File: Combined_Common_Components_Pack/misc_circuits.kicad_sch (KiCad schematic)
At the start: 26 parts, among them Q10 2N7002K, Q11 2N7002K, Q9 PMOS, U8 FM8002

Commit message: More circuits
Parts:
- removed PROG2: SW_Push, Button_Switch_SMD:SW_SPST_PTS647_Sx38, symbol Switch:SW_Push
- added Batt3: Conn_01x02_Socket, Connector_Molex:Molex_KK-254_AE-6410-02A_1x02_P2.54mm_Vertical, symbol Connector:Conn_01x02_Socket
- added C47: 1nF, Capacitor_SMD:C_0805_2012Metric, symbol 1_Library_GF:C_THT_RECT
- added C48: 10u, Capacitor_SMD:C_0805_2012Metric, symbol Device:C
- added C49: 47nF, Capacitor_THT:C_Rect_L11.0mm_W4.3mm_P10.00mm_MKT, symbol 1_Library_GF:C_THT_RECT
- added C50: 10nF, Capacitor_THT:C_Rect_L7.0mm_W3.5mm_P5.00mm, symbol 1_Library_GF:C_THT_RECT
- added C51: 100n, Capacitor_SMD:C_0603_1608Metric, symbol Device:C
- added D28, D30, D31, D32, D33: SM4007, Diode_SMD:D_MELF, symbol Diode:SM4007
- added D29: LED, LED_SMD:LED_0805_2012Metric_Pad1.15x1.40mm_HandSolder, symbol Device:LED
- added D36, D37: LED, LED_SMD:LED_0805_2012Metric, symbol Device:LED
- added D38, D39: PTVS5V0Z1USK, Diode_SMD:Nexperia_DSN1608-2_1.6x0.8mm, symbol Diode:PTVS5V0Z1USK
- added LOAD1: Conn_01x02_Pin, Connector_Phoenix_GMSTB:PhoenixContact_GMSTBA_2,5_2-G-7,62_1x02_P7.62mm_Horizontal, symbol Connector:Conn_01x02_Pin
- added P1: USB_C_Plug_USB2.0, Connector_USB:USB_C_Receptacle_HRO_TYPE-C-31-M-12, symbol Connector:USB_C_Plug_USB2.0
- added Q13: BTA16-600B, Package_TO_SOT_THT:TO-220-3_Vertical, symbol Triac_Thyristor:BTA16-600B
- added Q14: BC817, Package_TO_SOT_SMD:SOT-23, symbol Transistor_BJT:BC817
- added Q15: 2N7002K, Package_TO_SOT_SMD:SOT-23, symbol Transistor_FET:2N7002K
- added Q16: FDS9926A, Package_SO:SOIC-8_3.9x4.9mm_P1.27mm, symbol Transistor_FET:FDS9926A
- added R100: 22k, Resistor_SMD:R_0805_2012Metric, symbol Device:R
- added R101: 10k, Resistor_SMD:R_0805_2012Metric, symbol Device:R
- added R102, R96: 360, Resistor_THT:R_Axial_DIN0411_L9.9mm_D3.6mm_P15.24mm_Horizontal, symbol Device:R
- added R103: 0R22, Resistor_SMD:R_2010_5025Metric, symbol Device:R
- added R104: 100, Resistor_SMD:R_0603_1608Metric, symbol Device:R
- added R105, R106, R109: 1k, Resistor_SMD:R_0603_1608Metric, symbol Device:R
- added R107, R108: 5k6, Resistor_SMD:R_0603_1608Metric, symbol Device:R
- added R110: 2k2, Resistor_SMD:R_0603_1608Metric, symbol Device:R
- added R90, R98: 220k, Resistor_SMD:R_0805_2012Metric, symbol Device:R
- added R91, R97: 1k, Resistor_SMD:R_0805_2012Metric, symbol Device:R
- added R92, R93, R94: 330, Resistor_SMD:R_0805_2012Metric, symbol Device:R
- added R95: 470, Resistor_THT:R_Axial_DIN0411_L9.9mm_D3.6mm_P15.24mm_Horizontal, symbol Device:R
- added R99: 39, Resistor_THT:R_Axial_DIN0411_L9.9mm_D3.6mm_P15.24mm_Horizontal, symbol Device:R
- added U13: PC817, Package_DIP:SMDIP-4_W7.62mm, symbol Isolator:PC817
- added U18: ~, Library:HEATSINK-TH_L34.0-W12.0, symbol New_Library:Heat Sink 34X12-25
- added U2: MOC3021M, Package_DIP:SMDIP-6_W9.53mm, symbol Relay_SolidState:MOC3021M
- added U20: TP4057, Package_TO_SOT_SMD:TSOT-23-5, symbol Battery_Management:TP4057
- added U21: DW01A, Package_TO_SOT_SMD:SOT-23-6, symbol Battery_Management:DW01A
- U8: Manufacturer FM(富满) -> (none); Supplier LCSC -> (none); Supplier Part C94625 -> (none)
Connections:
- net +3.3V: now also D29.2 (A), R92.1, R93.1
- net +BATT: now also Batt3.1 (Pin_1), R104.2, U20.3 (BAT)
- net GND: now also D38.2 (A), D39.2 (A), P1.A1 (GND), P1.A12 (GND), P1.B1 (GND), P1.B12 (GND), P1.S1 (SHIELD), Q15.2 (S), Q16.1 (S1), R101.2, R107.1, R108.1, R109.1, R110.1, U13.3, U20.2 (GND)
- new net: C47.1, D30.2 (A), D31.1 (K), R98.1
- new net: D31.2 (A), D32.1 (K), D33.2 (A), Q14.1 (B), R100.2
- new net: R105.1, U20.5 (STDBY)
- new net: D36.1 (K), R105.2
- new net: LOAD1.2 (Pin_2), Q13.2 (A2), R96.2, R99.2
- new net: Q13.3 (G), R102.2, U2.4
- new net: Q15.1 (G), R101.1, R94.2
- new net: Q16.4 (G2), U21.1 (OD)
- new net: R109.2, U21.2 (CS)
- new net: Q16.2 (G1), U21.3 (OC)
- new net: C51.1, R104.1, U21.5 (VCC)
- new net: Batt3.2 (Pin_2), C51.2, Q16.3 (S2), U21.6 (GND)
- new net: C48.1, D28.1 (K), D30.1 (K), R100.1, R91.1
- new net: C47.2, D28.2 (A), D33.1 (K), R90.1
- new net: R91.2, U13.1
- new net: Q14.3 (C), U13.2
- new net: P1.B5 (VCONN), R107.2
- new net: R106.1, U20.1 (~{CHRG})
- new net: D37.1 (K), R106.2
- new net: Q16.5 (D2), Q16.6 (D2), Q16.7 (D1), Q16.8 (D1)
- new net: C50.2, R99.1
- new net: C48.2, D32.2 (A), Q14.2 (E)
- new net: R92.2, R93.2, U2.1
- new net: Q15.3 (D), U2.2
- new net: R95.2, U2.6
- new net: P1.A5 (CC), R108.2
- new net: C49.1, R95.1, R96.1
- new net: R110.2, U20.6 (PROG)
- new net: R103.2, U20.4 (V_{CC})
- new net: D29.1 (K), R97.2
- new net D+: D38.1 (K), P1.A6 (D+)
- new net D-: D39.1 (K), P1.A7 (D-)
- new net TRIAC: R94.1
- new net VBUS: D36.2 (A), D37.2 (A), P1.A4 (VBUS), P1.A9 (VBUS), P1.B4 (VBUS), P1.B9 (VBUS), R103.1
- new net cold: LOAD1.1 (Pin_1), R98.2
- new net hot: C49.2, C50.1, Q13.1 (A1), R102.1, R90.2
- new net mainDet: R97.1, U13.4
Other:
- note added: "12P USB-C 1S charger + BMS"
- note added: "Auto reset serial programmer"
- note added: "V(AC) Driver"
- note added: "Zero-crossing detector"
- note removed: "Auto reset"
- moved on the sheet: C35, C36, C37, C38, C44, C46, D20, D25, PROG1, Q9, R73, R74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

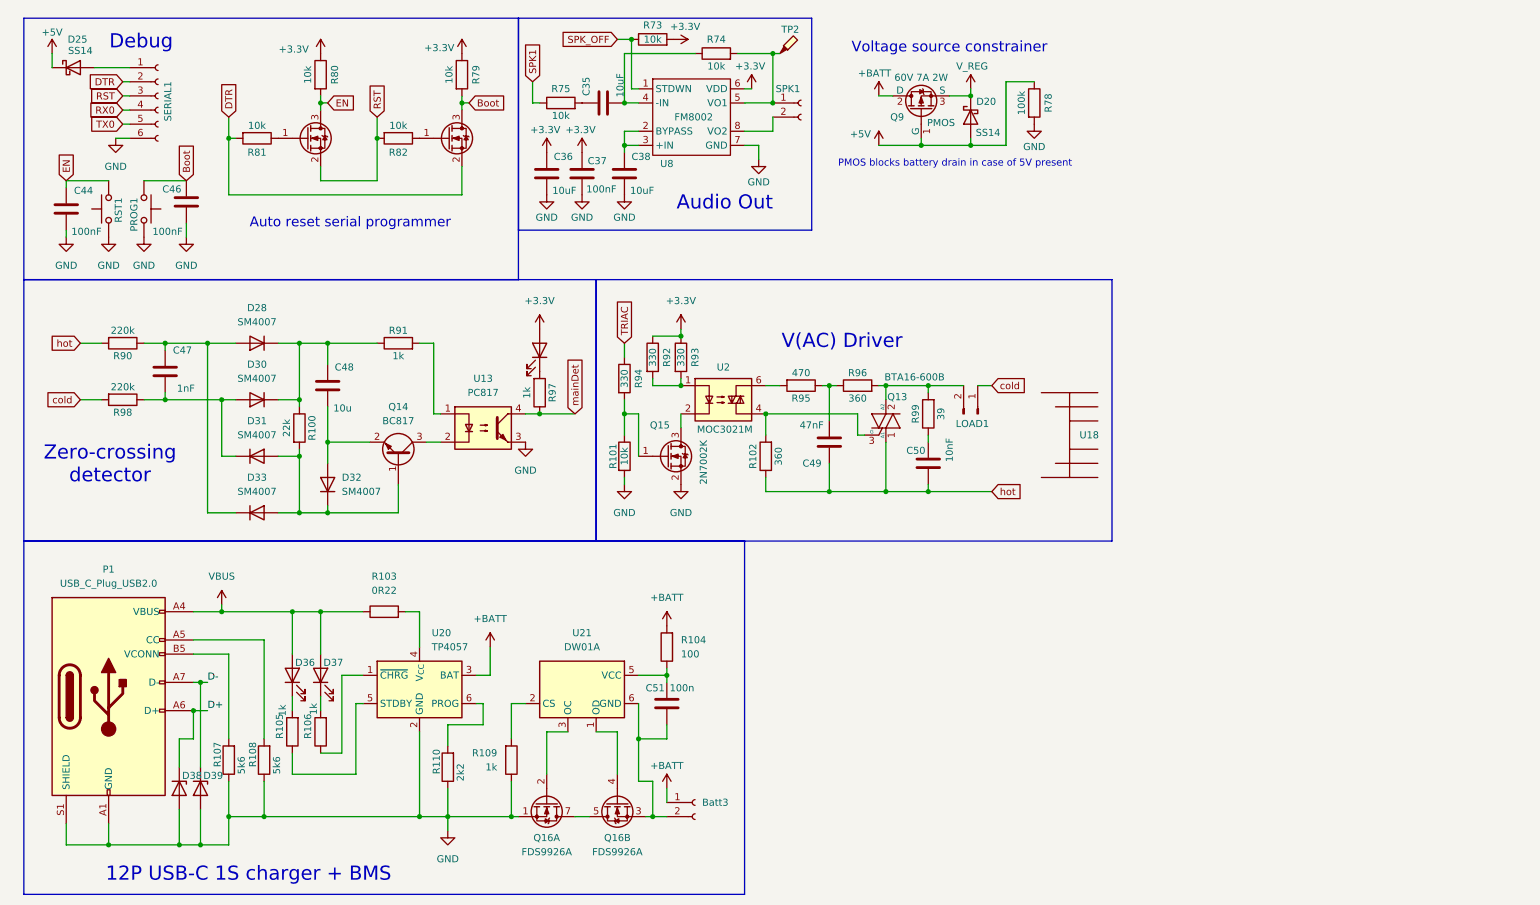
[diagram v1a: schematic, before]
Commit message: Minor updates
Basically components annotation, and more basic parts added
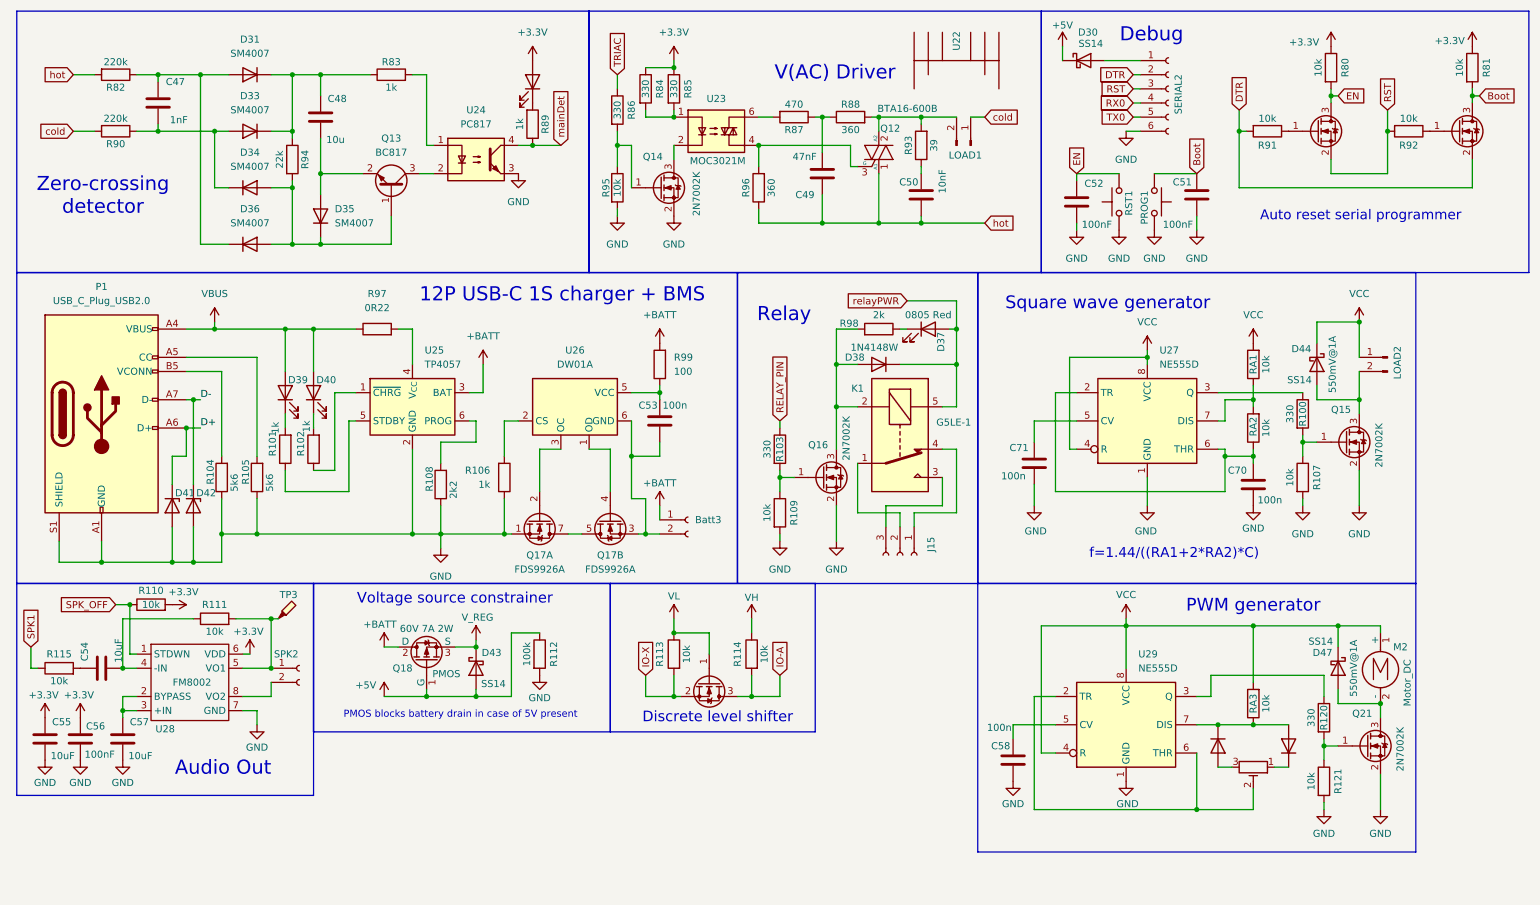
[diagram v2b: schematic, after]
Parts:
- added C58, C70, C71: 100n, Capacitor_SMD:C_0805_2012Metric, symbol Device:C
- added D37: LED_RED, LED_SMD:LED_0805_2012Metric_Pad1.15x1.40mm_HandSolder, symbol Device:LED
- added D38, D45, D46: 1N4148W, Diode_SMD:D_SOD-123, symbol Diode:1N4148W
- added D44, D47: SS14, Diode_SMD:D_SMA, symbol Diode:SS14
- added J15: Conn_01x03_Socket, Connector_JST:JST_NV_B03P-NV_1x03_P5.00mm_Vertical, symbol Connector:Conn_01x03_Socket
- added K1: G5LE-1, Relay_THT:Relay_SPDT_Omron-G5LE-1, symbol Relay:G5LE-1
- added LOAD2: Conn_01x02_Pin, Connector_Phoenix_GMSTB:PhoenixContact_GMSTBA_2,5_2-G-7,62_1x02_P7.62mm_Horizontal, symbol Connector:Conn_01x02_Pin
- added M2: Motor_DC, symbol Motor:Motor_DC
- added Q15, Q16, Q19, Q21: 2N7002K, Package_TO_SOT_SMD:SOT-23, symbol Transistor_FET:2N7002K
- added R100, R103, R120: 330, Resistor_SMD:R_0805_2012Metric, symbol Device:R
- added R107, R109, R121, RA1, RA2, RA3: 10k, Resistor_SMD:R_0805_2012Metric, symbol Device:R
- added R113, R114: 10k, Resistor_SMD:R_0402_1005Metric, symbol Device:R
- added R98: 2k, Resistor_SMD:R_0402_1005Metric_Pad0.72x0.64mm_HandSolder, symbol 1_Library_GF:R_SMD_0805
- added RV2: 10k, Potentiometer_THT:Potentiometer_Runtron_RM-065_Vertical, symbol Device:R_Potentiometer_Trim
- added U27, U29: NE555D, Package_SO:SOIC-8_3.9x4.9mm_P1.27mm, symbol Timer:NE555D
- renumbered C46 to C51, C44 to C52, C51 to C53, C35 to C54, C36 to C55, C37 to C56, C38 to C57, D25 to D30, D28 to D31, D29 to D32, D30 to D33, D31 to D34, D32 to D35, D33 to D36, D36 to D39, D37 to D40, D38 to D41, D39 to D42, D20 to D43, Q13 to Q12, Q14 to Q13, Q15 to Q14, Q16 to Q17, Q9 to Q18, R105 to R101, R106 to R102, R107 to R104, R108 to R105, R109 to R106, R110 to R108, R73 to R110, R74 to R111, R78 to R112, R75 to R115, R79 to R81, R90 to R82, R91 to R83, R92 to R84, R93 to R85, R94 to R86, R95 to R87, R96 to R88, R97 to R89, R98 to R90, R81 to R91, R82 to R92, R99 to R93, R100 to R94, R101 to R95, R102 to R96, R103 to R97, R104 to R99, SERIAL1 to SERIAL2, SPK1 to SPK2, TP2 to TP3, U18 to U22, U2 to U23, U13 to U24, U20 to U25, U21 to U26, U8 to U28
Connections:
- net GND: now also C58.1, C70.1, C71.1, Q15.2 (S), Q16.2 (S), Q21.2 (S), R107.2, R109.2, R121.2, U27.1 (GND), U29.1 (GND)
- new net: Q21.1 (G), R120.2, R121.1
- new net: Q15.1 (G), R100.2, R107.1
- new net: D44.2 (A), LOAD2.2 (Pin_2), Q15.3 (D)
- new net: D37.1 (K), R98.1
- new net: RV2.2, U29.2 (TR), U29.6 (THR)
- new net: R120.1, U29.3 (Q)
- new net: C58.2, U29.5 (CV)
- new net: D45.1 (K), D46.2 (A), RA3.1, U29.7 (DIS)
- new net: J15.2 (Pin_2), K1.1
- new net: D38.2 (A), K1.2, Q16.3 (D), R98.2
- new net: J15.3 (Pin_3), K1.3
- new net: J15.1 (Pin_1), K1.4
- new net: D47.2 (A), M2.2 (-), Q21.3 (D)
- new net: C70.2, RA2.1, U27.2 (TR), U27.6 (THR)
- new net: RA1.1, RA2.2, U27.7 (DIS)
- new net: D46.1 (K), RV2.1
- new net: D45.2 (A), RV2.3
- new net: Q16.1 (G), R103.2, R109.1
- new net: R100.1, U27.3 (Q)
- new net: C71.2, U27.5 (CV)
- new net IO-A: Q19.3 (D), R114.2
- new net IO-X: Q19.2 (S), R113.2
- new net RELAY_PIN: R103.1
- new net VCC: D44.1 (K), D47.1 (K), LOAD2.1 (Pin_1), M2.1 (+), RA1.2, RA3.2, U27.4 (R), U27.8 (VCC), U29.4 (R), U29.8 (VCC)
- new net VH: R114.1
- new net VL: Q19.1 (G), R113.1
- new net relayPWR: D37.2 (A), D38.1 (K), K1.5
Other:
- note added: "Discrete level shifter"
- note added: "PWM generator"
- note added: "Relay"
- note added: "Square wave generator"
- note added: "f=1.44/((RA1+2*RA2)*C)"
- moved on the sheet: Batt3, C47, C48, C49, C50, C51, C52, C53, C54, C55, C56, C57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

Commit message: Minor updates
Started footprint library for easier cross-computer design management.
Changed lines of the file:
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@@
 (kicad_sch
-	(version 20231120)
+	(version 20250114)
 	(generator "eeschema")
-	(generator_version "8.0")
+	(generator_version "9.0")
 	(paper "A4")
+	(rectangle
+		(start 66.04 115.57)
+		(end 119.38 142.24)
+		(stroke
+			(width 0)
+			(type default)
+		)
+		(fill
+			(type none)
+		)
+	)
+	(rectangle
+		(start 12.7 115.57)
+		(end 66.04 153.67)
+		(stroke
+			(width 0)
+			(type default)
+		)
+		(fill
+			(type none)
+		)
+	)
+	(rectangle
+		(start 196.85 12.7)
+		(end 284.48 59.69)
+		(stroke
+			(width 0)
+			(type default)
+		)
+		(fill
+			(type none)
+		)
+	)
+	(rectangle
+		(start 115.57 12.7)
+		(end 196.85 59.69)
+		(stroke
+			(width 0)
+			(type default)
+		)
+		(fill
+			(type none)
+		)
+	)
+	(rectangle
+		(start 12.7 59.69)
+		(end 142.24 115.57)
+		(stroke
+			(width 0)
+			(type default)
+		)
+		(fill
+			(type none)
+		)
+	)
+	(rectangle
+		(start 185.42 115.57)
+		(end 264.16 163.83)
+		(stroke
+			(width 0)
+			(type default)
+		)
+		(fill
+			(type none)
+		)
+	)
+	(rectangle
+		(start 142.24 59.69)
+		(end 185.42 115.57)
+		(stroke
+			(width 0)
+			(type default)
+		)
+		(fill
+			(type none)
+		)
+	)
+	(rectangle
+		(start 119.38 115.57)
+		(end 156.21 142.24)
+		(stroke
+			(width 0)
+			(type default)
+		)
+		(fill
+			(type none)
+		)
+	)
+	(rectangle
+		(start 12.7 12.7)
+		(end 115.57 59.69)
+		(stroke
+			(width 0)
+			(type default)
+		)
+		(fill
+			(type none)
+		)
+	)
+	(rectangle
+		(start 185.42 59.69)
+		(end 264.16 115.57)
+		(stroke
+			(width 0)
+			(type default)
+		)
+		(fill
+			(type none)
+		)
+	)
+	(text "Discrete level shifter"
+		(exclude_from_sim no)
+		(at 138.684 139.7 0)
+		(effects
+			(font
+				(size 1.905 1.905)
+			)
+		)
+	)
+	(text "Audio Out"
+		(exclude_from_sim no)
+		(at 49.784 148.844 0)
+		(effects
+			(font
+				(size 2.54 2.54)
+			)
+		)
+	)
+	(text "12P USB-C 1S charger + BMS"
+		(exclude_from_sim no)
+		(at 110.744 63.754 0)
+		(effects
+			(font
+				(size 2.54 2.54)
+			)
+		)
+	)
+	(text "Voltage source constrainer"
+		(exclude_from_sim no)
+		(at 91.44 118.364 0)
+		(effects
+			(font
+				(size 1.905 1.905)
+			)
+		)
+	)
+	(text "Square wave generator"
+		(exclude_from_sim no)
+		(at 208.788 65.278 0)
+		(effects
+			(font
+				(size 2.286 2.286)
+			)
+		)
+	)
+	(text "PMOS blocks battery drain in case of 5V present"
+		(exclude_from_sim no)
+		(at 92.456 139.192 0)
+		(effects
+			(font
+				(size 1.27 1.27)
+			)
+		)
+	)
+	(text "f=1.44/((RA1+2*RA2)*C)"
+		(exclude_from_sim no)
+		(at 220.726 110.236 0)
+		(effects
+			(font
+				(size 1.778 1.778)
+			)
+		)
+	)
+	(text "Relay"
+		(exclude_from_sim no)
+		(at 150.622 67.31 0)
+		(effects
+			(font
+				(size 2.54 2.54)
+			)
+		)
+	)
+	(text "Zero-crossing\ndetector"
+		(exclude_from_sim no)
+		(at 28.194 45.974 0)
+		(effects
+			(font
+				(size 2.54 2.54)
+			)
+		)
+	)
+	(text "Auto reset serial programmer"
+		(exclude_from_sim no)
+		(at 254.254 49.53 0)
+		(effects
+			(font
+				(size 1.778 1.778)
+			)
+		)
+	)
+	(text "PWM generator"
+		(exclude_from_sim no)
+		(at 234.95 119.634 0)
+		(effects
+			(font
+				(size 2.286 2.286)
+			)
+		)
+	)
+	(text "Debug"
+		(exclude_from_sim no)
+		(at 216.662 17.018 0)
+		(effects
+			(font
+				(size 2.54 2.54)
+			)
+		)
+	)
+	(text "V(AC) Driver"
+		(exclude_from_sim no)
+		(at 159.766 23.876 0)
+		(effects
+			(font
+				(size 2.54 2.54)
+			)
+		)
+	)
 	(junction
 		(at 67.31 54.61)
@@
 		)
 	)
-	(rectangle
-		(start 66.04 115.57)
-		(end 119.38 142.24)
-		(stroke
-			(width 0)
-			(type default)
-		)
-		(fill
-			(type none)
-		)
-	)
-	(rectangle
-		(start 12.7 115.57)
-		(end 66.04 153.67)
-		(stroke
-			(width 0)
-			(type default)
-		)
-		(fill
-			(type none)
-		)
-	)
-	(rectangle
-		(start 196.85 12.7)
-		(end 284.48 59.69)
-		(stroke
-			(width 0)
-			(type default)
-		)
-		(fill
-			(type none)
-		)
-	)
-	(rectangle
-		(start 115.57 12.7)
-		(end 196.85 59.69)
-		(stroke
-			(width 0)
-			(type default)
-		)
-		(fill
-			(type none)
-		)
-	)
-	(rectangle
-		(start 12.7 59.69)
-		(end 142.24 115.57)
-		(stroke
-			(width 0)
-			(type default)
-		)
-		(fill
-			(type none)
-		)
-	)
-	(rectangle
-		(start 185.42 115.57)
-		(end 264.16 163.83)
-		(stroke
-			(width 0)
-			(type default)
-		)
-		(fill
-			(type none)
-		)
-	)
-	(rectangle
-		(start 142.24 59.69)
-		(end 185.42 115.57)
-		(stroke
-			(width 0)
-			(type default)
-		)
-		(fill
-			(type none)
-		)
-	)
-	(rectangle
-		(start 119.38 115.57)
-		(end 156.21 142.24)
-		(stroke
-			(width 0)
-			(type default)
-		)
-		(fill
-			(type none)
-		)
-	)
-	(rectangle
-		(start 12.7 12.7)
-		(end 115.57 59.69)
-		(stroke
-			(width 0)
-			(type default)
-		)
-		(fill
-			(type none)
-		)
-	)
-	(rectangle
-		(start 185.42 59.69)
-		(end 264.16 115.57)
-		(stroke
-			(width 0)
-			(type default)
-		)
-		(fill
-			(type none)
-		)
-	)
-	(text "Discrete level shifter"
-		(exclude_from_sim no)
-		(at 138.684 139.7 0)
-		(effects
-			(font
-				(size 1.905 1.905)
-			)
-		)
-	)
-	(text "Audio Out"
-		(exclude_from_sim no)
-		(at 49.784 148.844 0)
-		(effects
-			(font
-				(size 2.54 2.54)
-			)
-		)
-	)
-	(text "12P USB-C 1S charger + BMS"
-		(exclude_from_sim no)
-		(at 110.744 63.754 0)
-		(effects
-			(font
-				(size 2.54 2.54)
-			)
-		)
-	)
-	(text "Voltage source constrainer"
-		(exclude_from_sim no)
-		(at 91.44 118.364 0)
-		(effects
-			(font
-				(size 1.905 1.905)
-			)
-		)
-	)
-	(text "Square wave generator"
-		(exclude_from_sim no)
-		(at 208.788 65.278 0)
-		(effects
-			(font
-				(size 2.286 2.286)
-			)
-		)
-	)
-	(text "PMOS blocks battery drain in case of 5V present"
-		(exclude_from_sim no)
-		(at 92.456 139.192 0)
-		(effects
-			(font
-				(size 1.27 1.27)
-			)
-		)
-	)
-	(text "f=1.44/((RA1+2*RA2)*C)"
-		(exclude_from_sim no)
-		(at 220.726 110.236 0)
-		(effects
-			(font
-				(size 1.778 1.778)
-			)
-		)
-	)
-	(text "Relay"
-		(exclude_from_sim no)
-		(at 150.622 67.31 0)
-		(effects
-			(font
-				(size 2.54 2.54)
-			)
-		)
-	)
-	(text "Zero-crossing\ndetector"
-		(exclude_from_sim no)
-		(at 28.194 45.974 0)
-		(effects
-			(font
-				(size 2.54 2.54)
-			)
-		)
-	)
-	(text "Auto reset serial programmer"
-		(exclude_from_sim no)
-		(at 254.254 49.53 0)
-		(effects
-			(font
-				(size 1.778 1.778)
-			)
-		)
-	)
-	(text "PWM generator"
-		(exclude_from_sim no)
-		(at 234.95 119.634 0)
-		(effects
-			(font
-				(size 2.286 2.286)
-			)
-		)
-	)
-	(text "Debug"
-		(exclude_from_sim no)
-		(at 216.662 17.018 0)
-		(effects
-			(font
-				(size 2.54 2.54)
-			)
-		)
-	)
-	(text "V(AC) Driver"
-		(exclude_from_sim no)
-		(at 159.766 23.876 0)
-		(effects
-			(font
-				(size 2.54 2.54)
-			)
-		)
-	)
